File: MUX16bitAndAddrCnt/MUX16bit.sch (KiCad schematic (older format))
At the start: 32 parts, among them J1 Conn_01x17_Female, J2 Conn_01x17_Female, J3 Conn_01x17_Female, J4 Conn_01x17_Female, J5 Conn_01x17_Female, J6 Conn_01x01_Male, J7 Conn_01x03_Male, J8 Screw_Terminal_01x02, Q1 IRLML5203, U1 MUX4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

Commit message: Address counter in work
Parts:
- added J9: Conn_01x09_Male, Connector_PinHeader_2.54mm:PinHeader_1x09_P2.54mm_Vertical, symbol Connector:Conn_01x09_Male
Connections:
- net BUS0 is gone; now on net O0: J5.16 (Pin_16)
- net BUS1 is gone; now on net O1: J5.15 (Pin_15)
- net BUS10 is gone; now on net O10: J5.6 (Pin_6)
- net BUS11 is gone; now on net O11: J5.5 (Pin_5)
- net BUS12 is gone; now on net O12: J5.4 (Pin_4)
- net BUS13 is gone; now on net O13: J5.3 (Pin_3)
- net BUS14 is gone; now on net O14: J5.2 (Pin_2)
- net BUS15 is gone; now on net O15: J5.1 (Pin_1)
- net BUS2 is gone; now on net O2: J5.14 (Pin_14)
- net BUS3 is gone; now on net O3: J5.13 (Pin_13)
- net BUS4 is gone; now on net O4: J5.12 (Pin_12)
- net BUS5 is gone; now on net O5: J5.11 (Pin_11)
- net BUS6 is gone; now on net O6: J5.10 (Pin_10)
- net BUS7 is gone; now on net O7: J5.9 (Pin_9)
- net BUS8 is gone; now on net O8: J5.8 (Pin_8)
- net BUS9 is gone; now on net O9: J5.7 (Pin_7)
- net ~OE is gone; now on an unnamed net: J6.1 (Pin_1)
- net D0: now also U13.9 (Q3)
- net D1: now also U13.12 (Q4)
- net D10: now also U14.15 (Q5)
- net D11: now also U14.6 (Q2)
- net D12: now also U14.5 (Q1)
- net D13: now also U14.16 (Q6)
- net D14: now also U14.19 (Q7)
- net D15: now also U14.2 (Q0)
- net D2: now also U13.15 (Q5)
- net D3: now also U13.6 (Q2)
- net D4: now also U13.5 (Q1)
- net D5: now also U13.16 (Q6)
- net D6: now also U13.19 (Q7)
- net D7: now also U13.2 (Q0)
- net D8: now also U14.9 (Q3)
- net D9: now also U14.12 (Q4)
- net GND: now also J9.9 (Pin_9)
- net CNST0: now reaches U11.10 (P0)
- net CNST0: now also J9.8 (Pin_8)
- net CNST1: now reaches U11.11 (P1)
- net CNST1: now also J9.7 (Pin_7)
- net CNST2: now reaches U11.12 (P2)
- net CNST2: now also J9.6 (Pin_6)
- net CNST3: now reaches U11.13 (P3)
- net CNST3: now also J9.5 (Pin_5)
- net CNST4: now reaches U11.14 (P4)
- net CNST4: now also J9.4 (Pin_4)
- net CNST5: now reaches U11.15 (P5)
- net CNST5: now also J9.3 (Pin_3)
- net CNST6: now reaches U11.16 (P6)
- net CNST6: now also J9.2 (Pin_2)
- net CNST7: now reaches U11.17 (P7)
- net CNST7: now also U12.10 (P0), U12.11 (P1), U12.12 (P2), U12.13 (P3), U12.14 (P4), U12.15 (P5), U12.16 (P6), U12.17 (P7), J9.1 (Pin_1)
- net N0: now reaches U11.18 (S0)
- net N0: now also U13.8 (D3); no longer U13.3 (D0)
- net N1: now reaches U11.19 (S1)
- net N1: now also U13.13 (D4); no longer U13.4 (D1)
- net N2: now reaches U11.20 (S2)
- net N2: now also U13.14 (D5); no longer U13.7 (D2)
- net N3: now reaches U11.21 (S3)
- net N3: now also U13.7 (D2); no longer U13.8 (D3)
- net N4: now reaches U11.22 (S4)
- net N4: now also U13.4 (D1); no longer U13.13 (D4)
- net N5: now reaches U11.23 (S5)
- net N5: now also U13.17 (D6); no longer U13.14 (D5)
- net N6: now reaches U11.24 (S6)
- net N6: now also U13.18 (D7); no longer U13.17 (D6)
- net N7: now reaches U11.25 (S7)
- net N7: now also U13.3 (D0); no longer U13.18 (D7)
- net N15: now reaches U14.3 (D0)
- net N15: now also U12.25 (S7); no longer U12.18 (S0)
- net N12: now reaches U14.4 (D1)
- net N12: now also U12.22 (S4); no longer U12.19 (S1)
- net N10: now reaches U12.20 (S2)
- net N10: now also U14.14 (D5); no longer U14.7 (D2)
- net N11: now reaches U12.21 (S3)
- net N11: now also U14.7 (D2); no longer U14.8 (D3)
- net N9: now reaches U14.13 (D4)
- net N9: now also U12.19 (S1); no longer U12.22 (S4)
- net N13: now reaches U12.23 (S5)
- net N13: now also U14.17 (D6); no longer U14.14 (D5)
- net N14: now reaches U12.24 (S6)
- net N14: now also U14.18 (D7); no longer U14.17 (D6)
- new net N8: U12.18 (S0), U14.8 (D3)
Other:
- note added: "High Addr"
- note added: "Low Addr"
- note added: "This is Cout pin.\nIt should be connected\nto Cin pin of U12 module."
- moved on the sheet: C1, C2, H1, H2, H3, H4, H5, H6, J1, J2, J3, J4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

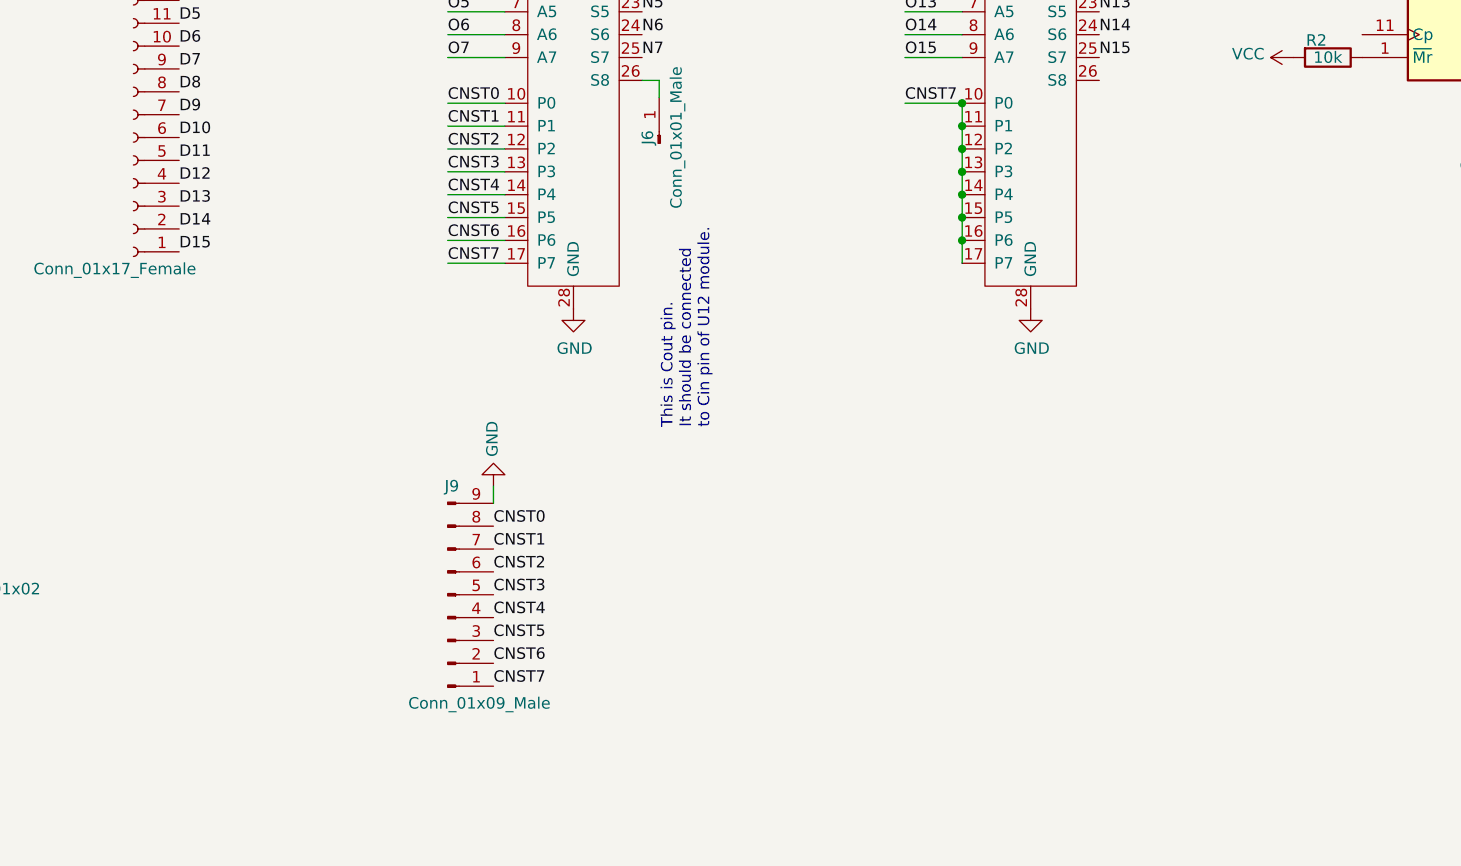
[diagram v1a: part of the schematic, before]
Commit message: Address counter in work
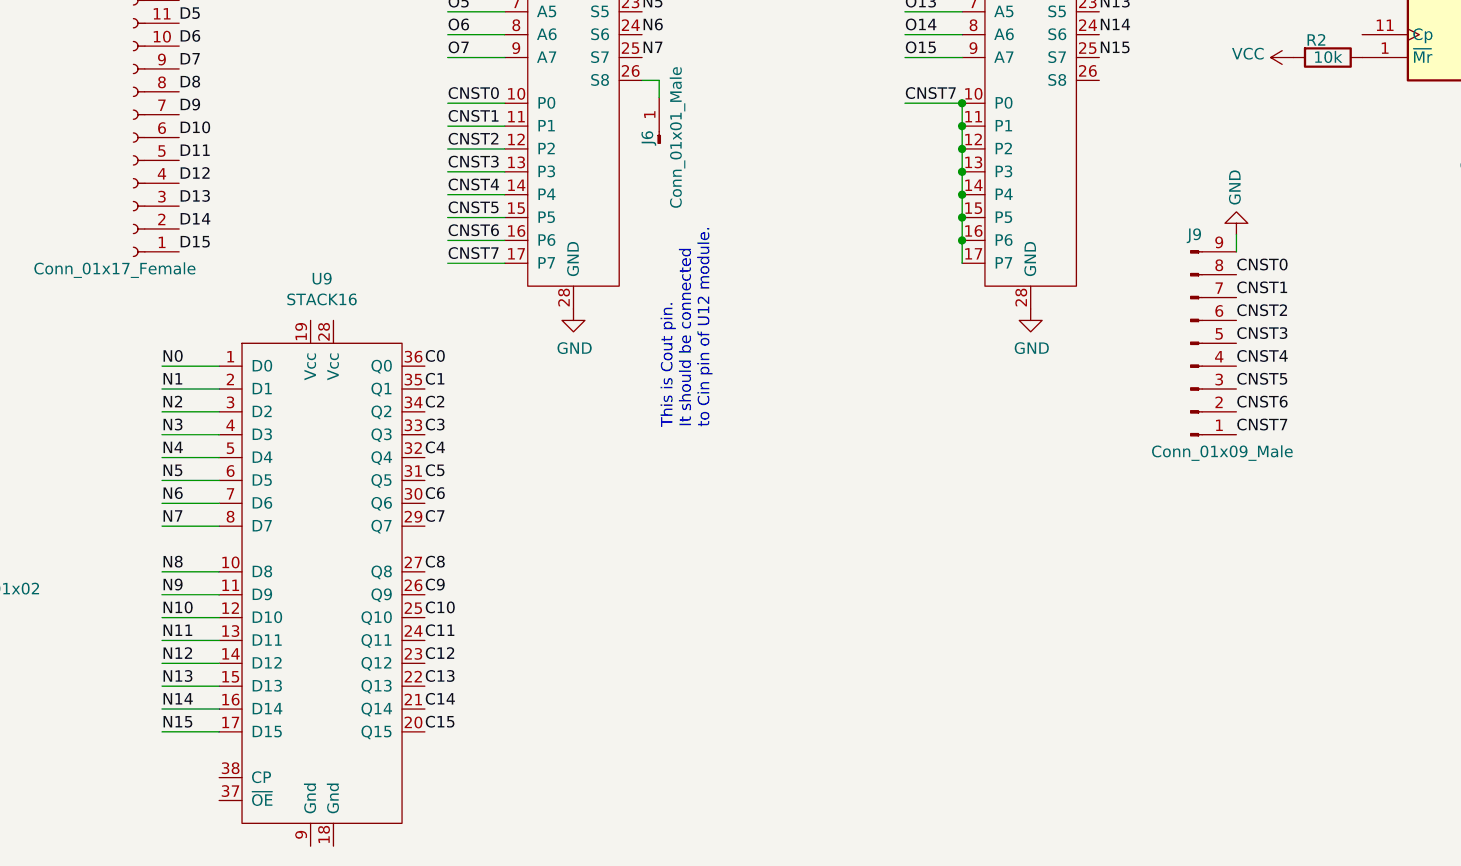
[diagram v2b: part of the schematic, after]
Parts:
- added U9: STACK16, CommonLibrary:STACK16, symbol CommonLibrary:STACK16
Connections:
- net C0: now also U9.36 (Q0)
- net C1: now also U9.35 (Q1)
- net C10: now also U9.25 (Q10)
- net C11: now also U9.24 (Q11)
- net C12: now also U9.23 (Q12)
- net C13: now also U9.22 (Q13)
- net C14: now also U9.21 (Q14)
- net C15: now also U9.20 (Q15)
- net C2: now also U9.34 (Q2)
- net C3: now also U9.33 (Q3)
- net C4: now also U9.32 (Q4)
- net C5: now also U9.31 (Q5)
- net C6: now also U9.30 (Q6)
- net C7: now also U9.29 (Q7)
- net C8: now also U9.27 (Q8)
- net C9: now also U9.26 (Q9)
- net N0: now also U9.1 (D0)
- net N1: now also U9.2 (D1)
- net N10: now also U9.12 (D10)
- net N11: now also U9.13 (D11)
- net N12: now also U9.14 (D12)
- net N13: now also U9.15 (D13)
- net N14: now also U9.16 (D14)
- net N15: now also U9.17 (D15)
- net N2: now also U9.3 (D2)
- net N3: now also U9.4 (D3)
- net N4: now also U9.5 (D4)
- net N5: now also U9.6 (D5)
- net N6: now also U9.7 (D6)
- net N7: now also U9.8 (D7)
- net N8: now also U9.10 (D8)
- net N9: now also U9.11 (D9)
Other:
- moved on the sheet: J9
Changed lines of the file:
@@
 L Connector:Conn_01x09_Male J9
 U 1 1 667594D7
-P 5500 6500
-F 0 "J9" H 5550 6025 50  0000 R CNN
-F 1 "Conn_01x09_Male" H 5950 6975 50  0000 R CNN
-F 2 "Connector_PinHeader_2.54mm:PinHeader_1x09_P2.54mm_Vertical" H 5500 6500 50  0001 C CNN
-F 3 "~" H 5500 6500 50  0001 C CNN
-	1    5500 6500
+P 8750 5400
+F 0 "J9" H 8800 4925 50  0000 R CNN
+F 1 "Conn_01x09_Male" H 9200 5875 50  0000 R CNN
+F 2 "Connector_PinHeader_2.54mm:PinHeader_1x09_P2.54mm_Vertical" H 8750 5400 50  0001 C CNN
+F 3 "~" H 8750 5400 50  0001 C CNN
+	1    8750 5400
 	1    0    0    1
 $EndComp
@@
 L power:GND #PWR0105
 U 1 1 667642DF
-P 5700 6025
-F 0 "#PWR0105" H 5700 5775 50  0001 C CNN
-F 1 "GND" V 5705 5897 50  0000 R CNN
-F 2 "" H 5700 6025 50  0001 C CNN
-F 3 "" H 5700 6025 50  0001 C CNN
-	1    5700 6025
+P 8950 4925
+F 0 "#PWR0105" H 8950 4675 50  0001 C CNN
+F 1 "GND" V 8955 4797 50  0000 R CNN
+F 2 "" H 8950 4925 50  0001 C CNN
+F 3 "" H 8950 4925 50  0001 C CNN
+	1    8950 4925
 	-1   0    0    1
 $EndComp
 Wire Wire Line
-	5700 6025 5700 6100
-Text Label 5700 6200 0    50   ~ 0
+	8950 4925 8950 5000
+Text Label 8950 5100 0    50   ~ 0
 CNST0
-Text Label 5700 6300 0    50   ~ 0
+Text Label 8950 5200 0    50   ~ 0
 CNST1
-Text Label 5700 6400 0    50   ~ 0
+Text Label 8950 5300 0    50   ~ 0
 CNST2
-Text Label 5700 6500 0    50   ~ 0
+Text Label 8950 5400 0    50   ~ 0
 CNST3
-Text Label 5700 6600 0    50   ~ 0
+Text Label 8950 5500 0    50   ~ 0
 CNST4
-Text Label 5700 6700 0    50   ~ 0
+Text Label 8950 5600 0    50   ~ 0
 CNST5
-Text Label 5700 6800 0    50   ~ 0
+Text Label 8950 5700 0    50   ~ 0
 CNST6
-Text Label 5700 6900 0    50   ~ 0
+Text Label 8950 5800 0    50   ~ 0
 CNST7
 Wire Wire Line
@@
 Text Label 9250 3850 0    50   ~ 0
 N14
+$Comp
+L CommonLibrary:STACK16 U9
+U 1 1 66718735
+P 4600 5400
+F 0 "U9" H 4950 5681 50  0000 C CNN
+F 1 "STACK16" H 4950 5590 50  0000 C CNN
+F 2 "CommonLibrary:STACK16" H 4600 5400 50  0001 C CNN
+F 3 "" H 4600 5400 50  0001 C CNN
+	1    4600 5400
+	1    0    0    -1
+$EndComp
+Wire Wire Line
+	4250 5500 4500 5500
+Wire Wire Line
+	4250 5600 4500 5600
+Wire Wire Line
+	4250 5700 4500 5700
+Wire Wire Line
+	4250 5800 4500 5800
+Wire Wire Line
+	4250 5900 4500 5900
+Wire Wire Line
+	4250 6000 4500 6000
+Wire Wire Line
+	4250 6100 4500 6100
+Wire Wire Line
+	4250 6200 4500 6200
+Text Label 4250 5500 0    50   ~ 0
+N0
+Text Label 4250 5600 0    50   ~ 0
+N1
+Text Label 4250 5700 0    50   ~ 0
+N2
+Text Label 4250 5800 0    50   ~ 0
+N3
+Text Label 4250 5900 0    50   ~ 0
+N4
+Text Label 4250 6000 0    50   ~ 0
+N5
+Text Label 4250 6100 0    50   ~ 0
+N6
+Text Label 4250 6200 0    50   ~ 0
+N7
+Wire Wire Line
+	4250 6400 4500 6400
+Wire Wire Line
+	4250 6500 4500 6500
+Wire Wire Line
+	4250 6600 4500 6600
+Wire Wire Line
+	4250 6700 4500 6700
+Wire Wire Line
+	4250 6800 4500 6800
+Wire Wire Line
+	4250 6900 4500 6900
+Wire Wire Line
+	4250 7000 4500 7000
+Wire Wire Line
+	4250 7100 4500 7100
+Text Label 4250 7100 0    50   ~ 0
+N15
+Text Label 4250 6800 0    50   ~ 0
+N12
+Text Label 4250 6700 0    50   ~ 0
+N11
+Text Label 4250 6400 0    50   ~ 0
+N8
+Text Label 4250 6500 0    50   ~ 0
+N9
+Text Label 4250 6600 0    50   ~ 0
+N10
+Text Label 4250 6900 0    50   ~ 0
+N13
+Text Label 4250 7000 0    50   ~ 0
+N14
+Text Label 5400 5500 0    50   ~ 0
+C0
+Text Label 5400 5600 0    50   ~ 0
+C1
+Text Label 5400 5700 0    50   ~ 0
+C2
+Text Label 5400 5800 0    50   ~ 0
+C3
+Text Label 5400 5900 0    50   ~ 0
+C4
+Text Label 5400 6000 0    50   ~ 0
+C5
+Text Label 5400 6100 0    50   ~ 0
+C6
+Text Label 5400 6200 0    50   ~ 0
+C7
+Text Label 5400 6400 0    50   ~ 0
+C8
+Text Label 5400 6500 0    50   ~ 0
+C9
+Text Label 5400 6600 0    50   ~ 0
+C10
+Text Label 5400 6700 0    50   ~ 0
+C11
+Text Label 5400 6800 0    50   ~ 0
+C12
+Text Label 5400 6900 0    50   ~ 0
+C13
+Text Label 5400 7000 0    50   ~ 0
+C14
+Text Label 5400 7100 0    50   ~ 0
+C15
 $EndSCHEMATC

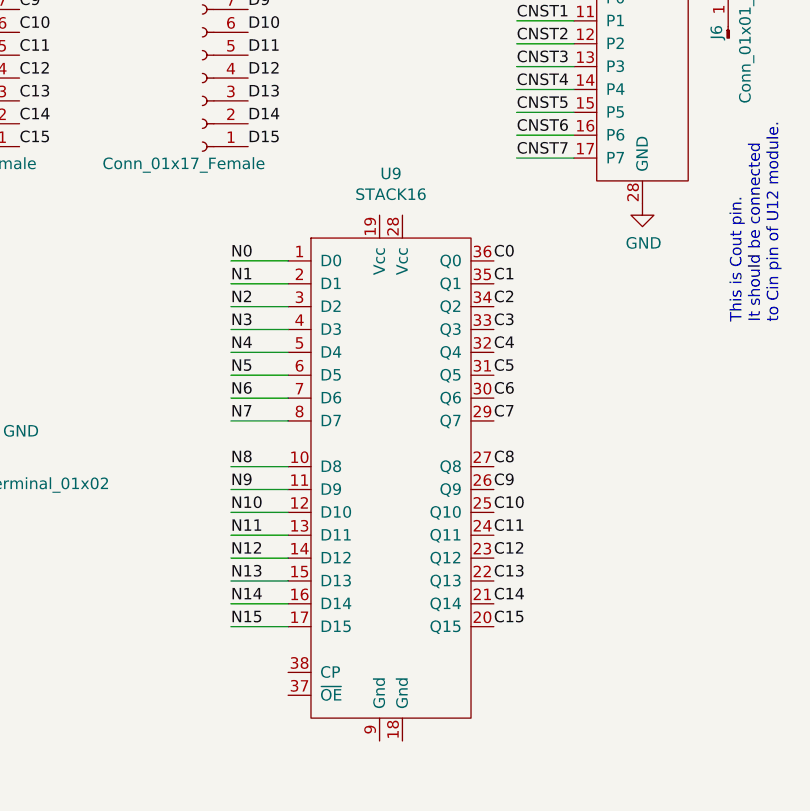
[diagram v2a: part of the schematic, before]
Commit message: Address counter in work
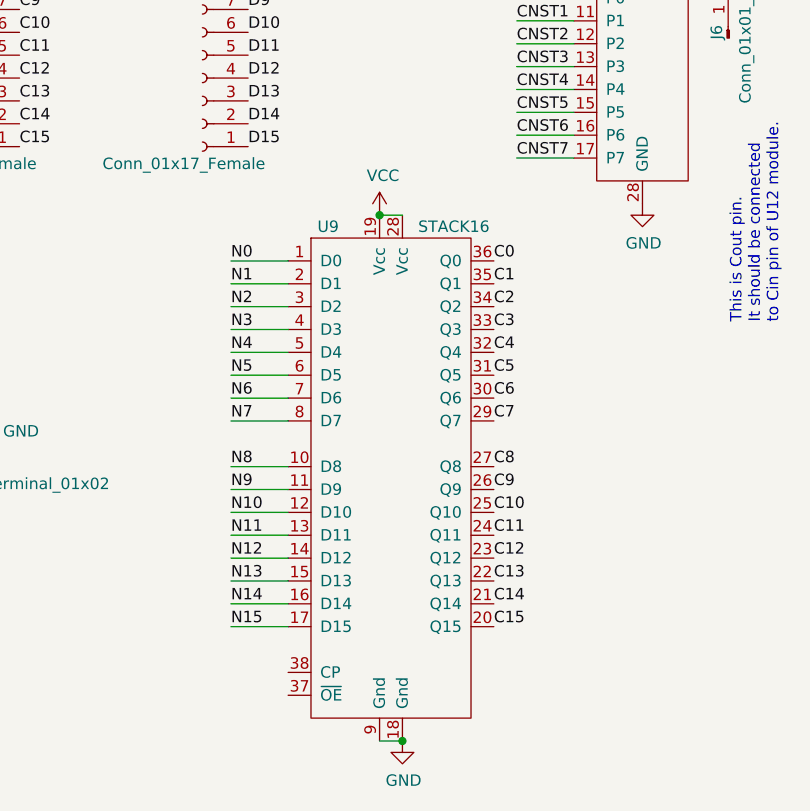
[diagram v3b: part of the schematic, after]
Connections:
- net GND: now also U9.18 (Gnd), U9.9 (Gnd)
- net VCC: now also U9.19 (Vcc), U9.28 (Vcc)
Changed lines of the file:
@@
 U 1 1 66718735
 P 4600 5400
-F 0 "U9" H 4950 5681 50  0000 C CNN
-F 1 "STACK16" H 4950 5590 50  0000 C CNN
+F 0 "U9" H 4675 5450 50  0000 C CNN
+F 1 "STACK16" H 5225 5450 50  0000 C CNN
 F 2 "CommonLibrary:STACK16" H 4600 5400 50  0001 C CNN
 F 3 "" H 4600 5400 50  0001 C CNN
@@
 Text Label 5400 7100 0    50   ~ 0
 C15
+$Comp
+L power:GND #PWR?
+U 1 1 6689E4FA
+P 5000 7600
+F 0 "#PWR?" H 5000 7350 50  0001 C CNN
+F 1 "GND" H 5005 7427 50  0000 C CNN
+F 2 "" H 5000 7600 50  0001 C CNN
+F 3 "" H 5000 7600 50  0001 C CNN
+	1    5000 7600
+	1    0    0    -1
+$EndComp
+Wire Wire Line
+	4900 7600 5000 7600
+Connection ~ 5000 7600
+$Comp
+L power:VCC #PWR?
+U 1 1 668AED81
+P 4900 5300
+F 0 "#PWR?" H 4900 5150 50  0001 C CNN
+F 1 "VCC" H 4915 5473 50  0000 C CNN
+F 2 "" H 4900 5300 50  0001 C CNN
+F 3 "" H 4900 5300 50  0001 C CNN
+	1    4900 5300
+	1    0    0    -1
+$EndComp
+Wire Wire Line
+	4900 5300 5000 5300
+Connection ~ 4900 5300
 $EndSCHEMATC

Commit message: Polishing Address counter
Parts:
- added J10, J11: Conn_01x01_Male, Connector_PinHeader_2.54mm:PinHeader_1x01_P2.54mm_Vertical, symbol Connector:Conn_01x01_Male
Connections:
- net +1\CNST: now also J10.1 (Pin_1)
- net GND: no longer U9.9 (Gnd)
- net VCC: no longer U9.28 (Vcc)
- net STEP: now reaches U13.11 (Cp)
- net STEP: now also U14.11 (Cp), J11.1 (Pin_1)
- no-connect marks 0 -> 5
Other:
- note added: "These pins have to be connected to "stack logic""
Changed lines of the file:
@@
 U 1 1 6486449B
 P 9350 2000
-F 0 "R1" V 9275 1950 50  0000 C CNN
+F 0 "R1" V 9425 1975 50  0000 C CNN
 F 1 "10k" V 9350 2000 50  0000 C CNN
 F 2 "Resistor_SMD:R_0805_2012Metric_Pad1.20x1.40mm_HandSolder" V 9280 2000 50  0001 C CNN
@@
 U 1 1 648927C5
 P 9350 4150
-F 0 "R2" V 9275 4100 50  0000 C CNN
+F 0 "R2" V 9425 4125 50  0000 C CNN
 F 1 "10k" V 9350 4150 50  0000 C CNN
 F 2 "Resistor_SMD:R_0805_2012Metric_Pad1.20x1.40mm_HandSolder" V 9280 4150 50  0001 C CNN
@@
 C15
 $Comp
-L power:GND #PWR?
+L power:GND #PWR0106
 U 1 1 6689E4FA
 P 5000 7600
-F 0 "#PWR?" H 5000 7350 50  0001 C CNN
+F 0 "#PWR0106" H 5000 7350 50  0001 C CNN
 F 1 "GND" H 5005 7427 50  0000 C CNN
 F 2 "" H 5000 7600 50  0001 C CNN
@@
 	1    0    0    -1
 $EndComp
-Wire Wire Line
-	4900 7600 5000 7600
-Connection ~ 5000 7600
-$Comp
-L power:VCC #PWR?
+$Comp
+L power:VCC #PWR0107
 U 1 1 668AED81
 P 4900 5300
-F 0 "#PWR?" H 4900 5150 50  0001 C CNN
+F 0 "#PWR0107" H 4900 5150 50  0001 C CNN
 F 1 "VCC" H 4915 5473 50  0000 C CNN
 F 2 "" H 4900 5300 50  0001 C CNN
@@
 	1    0    0    -1
 $EndComp
-Wire Wire Line
-	4900 5300 5000 5300
-Connection ~ 4900 5300
+NoConn ~ 5000 5300
+NoConn ~ 4900 7600
+NoConn ~ 8350 4250
+$Comp
+L Connector:Conn_01x01_Male J10
+U 1 1 66794AD6
+P 7250 5750
+F 0 "J10" H 7275 5800 50  0000 C CNN
+F 1 "Conn_01x01_Male" H 7275 5675 50  0000 C CNN
+F 2 "Connector_PinHeader_2.54mm:PinHeader_1x01_P2.54mm_Vertical" H 7250 5750 50  0001 C CNN
+F 3 "~" H 7250 5750 50  0001 C CNN
+	1    7250 5750
+	1    0    0    -1
+$EndComp
+$Comp
+L Connector:Conn_01x01_Male J11
+U 1 1 66795F85
+P 7250 6000
+F 0 "J11" H 7275 6050 50  0000 C CNN
+F 1 "Conn_01x01_Male" H 7275 5925 50  0000 C CNN
+F 2 "Connector_PinHeader_2.54mm:PinHeader_1x01_P2.54mm_Vertical" H 7250 6000 50  0001 C CNN
+F 3 "~" H 7250 6000 50  0001 C CNN
+	1    7250 6000
+	1    0    0    -1
+$EndComp
+Text Label 7450 5750 0    50   ~ 0
++1\CNST
+Wire Wire Line
+	9250 1900 9500 1900
+Text Label 9250 1900 0    50   ~ 0
+STEP
+Text Label 9250 4050 0    50   ~ 0
+STEP
+Wire Wire Line
+	9250 4050 9500 4050
+Text Label 7450 6000 0    50   ~ 0
+STEP
+NoConn ~ 4500 7300
+NoConn ~ 4500 7400
+Text Notes 2525 7375 0    50   ~ 0
+These pins have to be connected to "stack logic"
 $EndSCHEMATC
